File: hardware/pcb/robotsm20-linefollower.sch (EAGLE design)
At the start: 141 parts, among them Q5 BSS138LT3G, Q6 BSS138LT3G, Q7 BSS138LT3G, Q8 BSS138LT3G, U1 STM32F405RG

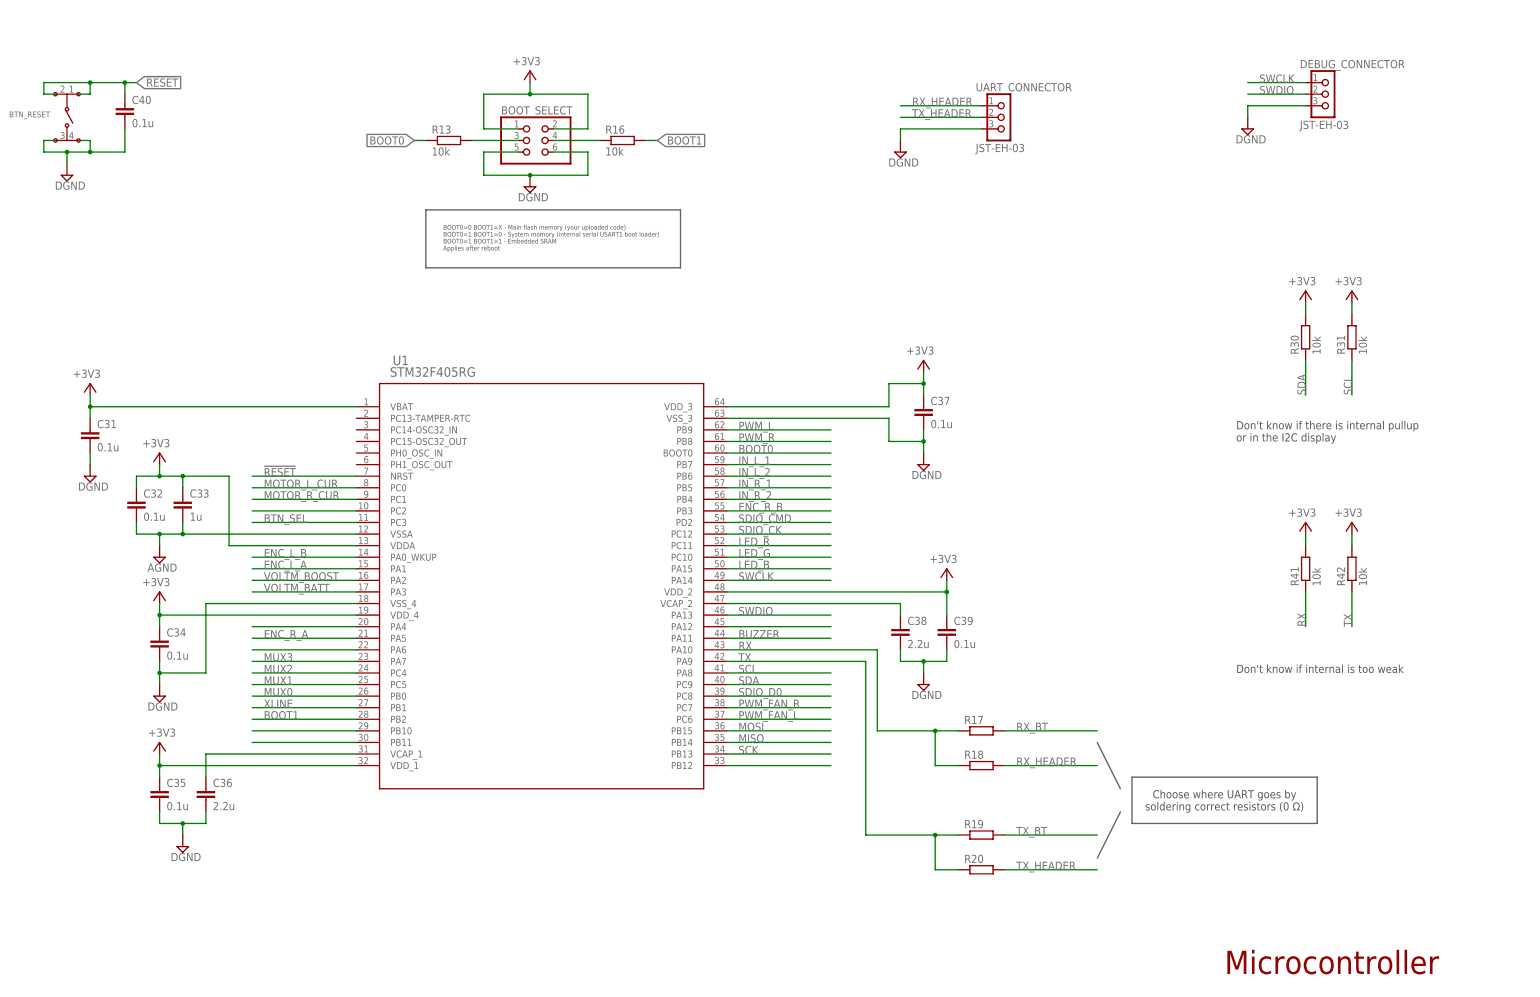
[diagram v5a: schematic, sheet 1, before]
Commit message: Change resistor and pinheader to dipswitch for RXTXBT and BOOT12
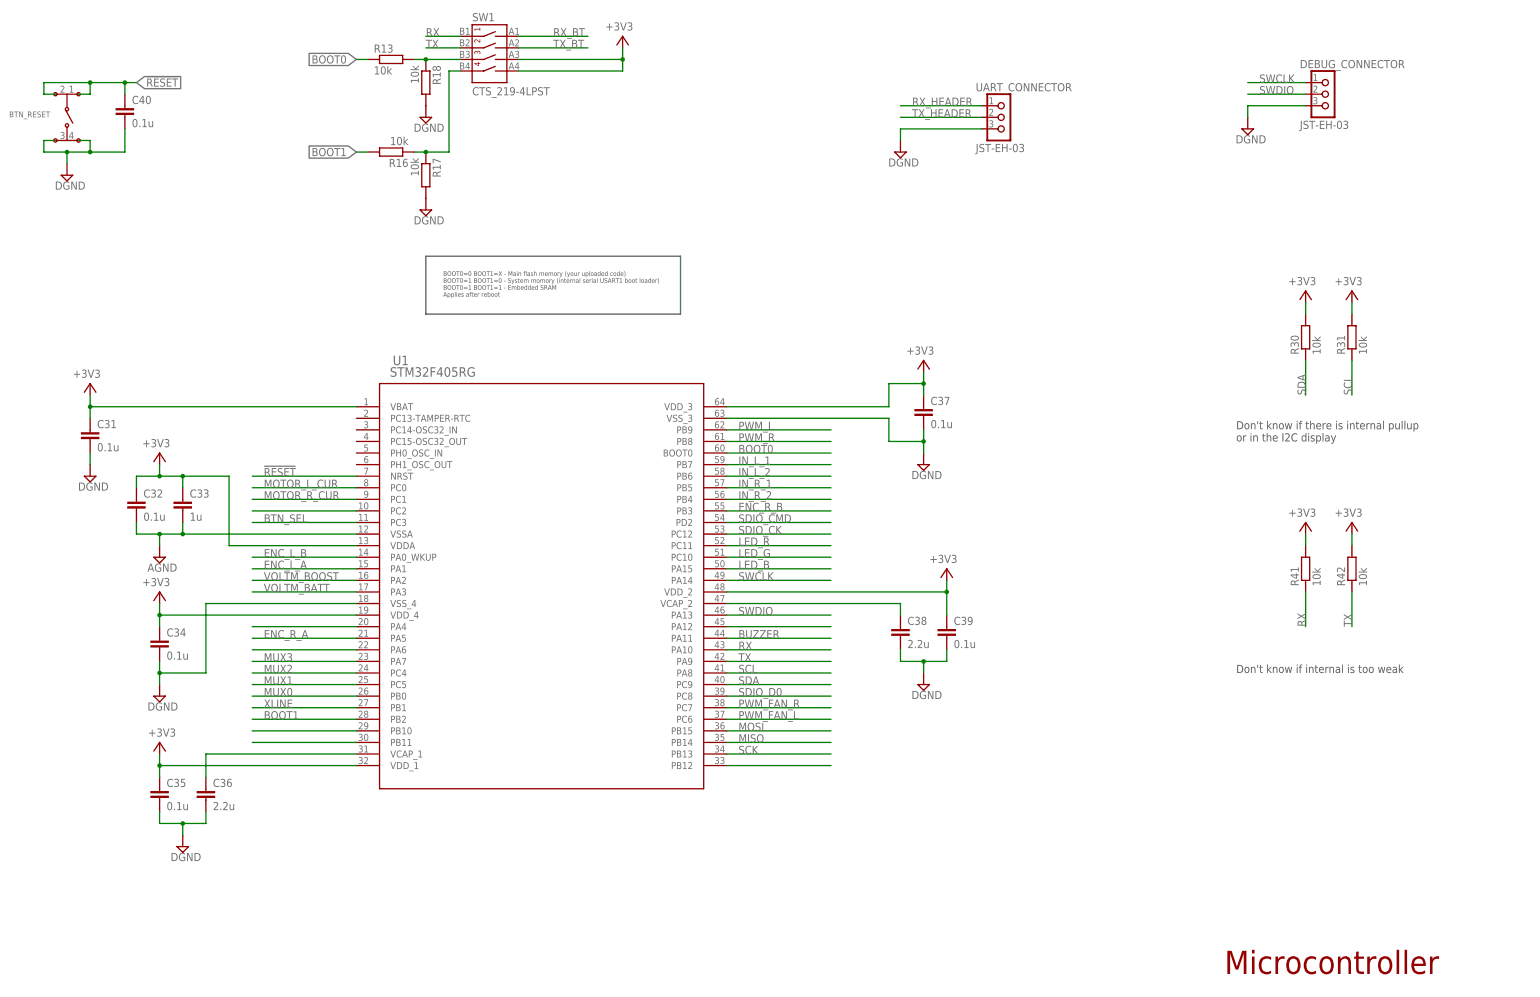
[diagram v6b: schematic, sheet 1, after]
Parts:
- removed BOOT_SELECT: (no value), CASE-Pinhead:PINHD-2X3
- removed R19, R20: (no value), rcl:R-EU_R0603
- added SW1: CTS_219-4LPST, CASE-Switches:CTS_219-4LPST
- R17, R18: value (none) -> 10k
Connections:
- net +3V3: now also SW1.A3, SW1.A4; no longer BOOT_SELECT.1, BOOT_SELECT.2
- net DGND: now also R17.1, R18.1; no longer BOOT_SELECT.5, BOOT_SELECT.6
- net N$26: now also R17.2, SW1.B4; no longer BOOT_SELECT.4
- net N$34: now also R18.2, SW1.B3; no longer BOOT_SELECT.3
- net RX: now also SW1.B1; no longer R17.2, R18.2
- net RX_BT: now also SW1.A1; no longer R17.1
- net RX_HEADER: no longer R18.1
- net TX: now also SW1.B2; no longer R19.2, R20.2
- net TX_BT: now also SW1.A2; no longer R19.1
- net TX_HEADER: no longer R20.1
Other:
- note removed: "Choose where UART goes by soldering correct resistors (0 Ω)"
- moved on the sheet: R13, R16, R17, R18

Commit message: Routed new dipswitch
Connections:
- removed net RX_HEADER: UART_CONNECTOR.1
- removed net TX_HEADER: UART_CONNECTOR.2
- net RX: now also UART_CONNECTOR.1
- net TX: now also UART_CONNECTOR.2
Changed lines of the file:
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@@
 <attribute name="VALUE" x="-167.767" y="70.485" size="1.778" layer="96"/>
 </instance>
-<instance part="SUPPLY48" gate="G$1" x="17.78" y="78.74" smashed="yes" grouprefs="UART">
-<attribute name="VALUE" x="15.113" y="75.565" size="1.778" layer="96"/>
+<instance part="SUPPLY48" gate="G$1" x="25.4" y="78.74" smashed="yes" grouprefs="UART">
+<attribute name="VALUE" x="22.733" y="75.565" size="1.778" layer="96"/>
 </instance>
 <instance part="SUPPLY49" gate="G$1" x="93.98" y="83.82" smashed="yes" grouprefs="DEBUG">
@@
 <attribute name="VALUE" x="-89.027" y="62.865" size="1.778" layer="96"/>
 </instance>
-<instance part="SW1" gate="G$1" x="-76.2" y="106.68" smashed="yes" rot="R270">
+<instance part="SW1" gate="G$1" x="-76.2" y="106.68" smashed="yes" rot="R270" grouprefs="MODE">
 <attribute name="NAME" x="-76.2" y="107.442" size="1.778" layer="95" font="vector"/>
 <attribute name="VALUE" x="-76.2" y="92.964" size="1.778" layer="96" font="vector" align="top-left"/>
@@
 <pinref part="SW1" gate="G$1" pin="B1"/>
 </segment>
+<segment>
+<pinref part="UART_CONNECTOR" gate="G$1" pin="1"/>
+<wire x1="35.56" y1="88.9" x2="25.4" y2="88.9" width="0.1524" layer="91" grouprefs="UART"/>
+<label x="27.94" y="88.9" size="1.778" layer="95" grouprefs="UART"/>
+</segment>
 </net>
 <net name="BUZZER" class="0">
@@
 <pinref part="SW1" gate="G$1" pin="B2"/>
 </segment>
+<segment>
+<pinref part="UART_CONNECTOR" gate="G$1" pin="2"/>
+<wire x1="35.56" y1="86.36" x2="25.4" y2="86.36" width="0.1524" layer="91" grouprefs="UART"/>
+<label x="27.94" y="86.36" size="1.778" layer="95" grouprefs="UART"/>
+</segment>
 </net>
 <net name="SDIO_D0" class="0">
@@
 <label x="-58.42" y="104.14" size="1.778" layer="95" grouprefs="MODE"/>
 <pinref part="SW1" gate="G$1" pin="A1"/>
-</segment>
-</net>
-<net name="RX_HEADER" class="0">
-<segment>
-<pinref part="UART_CONNECTOR" gate="G$1" pin="1"/>
-<wire x1="35.56" y1="88.9" x2="17.78" y2="88.9" width="0.1524" layer="91" grouprefs="UART"/>
-<label x="20.32" y="88.9" size="1.778" layer="95" grouprefs="UART"/>
-</segment>
-</net>
-<net name="TX_HEADER" class="0">
-<segment>
-<pinref part="UART_CONNECTOR" gate="G$1" pin="2"/>
-<wire x1="35.56" y1="86.36" x2="17.78" y2="86.36" width="0.1524" layer="91" grouprefs="UART"/>
-<label x="20.32" y="86.36" size="1.778" layer="95" grouprefs="UART"/>
 </segment>
 </net>
@@
 <junction x="-86.36" y="78.74" grouprefs="MODE"/>
 <pinref part="SW1" gate="G$1" pin="B4"/>
-<wire x1="-78.74" y1="96.52" x2="-81.28" y2="96.52" width="0.1524" layer="91"/>
-<wire x1="-81.28" y1="96.52" x2="-81.28" y2="78.74" width="0.1524" layer="91"/>
+<wire x1="-78.74" y1="96.52" x2="-81.28" y2="96.52" width="0.1524" layer="91" grouprefs="MODE"/>
+<wire x1="-81.28" y1="96.52" x2="-81.28" y2="78.74" width="0.1524" layer="91" grouprefs="MODE"/>
 </segment>
 </net>
@@
 <wire x1="-86.36" y1="99.06" x2="-88.9" y2="99.06" width="0.1524" layer="91" grouprefs="MODE"/>
 <pinref part="SW1" gate="G$1" pin="B3"/>
-<wire x1="-78.74" y1="99.06" x2="-86.36" y2="99.06" width="0.1524" layer="91"/>
-<junction x="-86.36" y="99.06"/>
+<wire x1="-78.74" y1="99.06" x2="-86.36" y2="99.06" width="0.1524" layer="91" grouprefs="MODE"/>
+<junction x="-86.36" y="99.06" grouprefs="MODE"/>
 </segment>
 </net>
@@
 <segment>
 <pinref part="+3V15" gate="G$1" pin="+3V3"/>
-<wire x1="-43.18" y1="101.6" x2="-43.18" y2="99.06" width="0.1524" layer="91"/>
+<wire x1="-43.18" y1="101.6" x2="-43.18" y2="99.06" width="0.1524" layer="91" grouprefs="MODE"/>
 <pinref part="SW1" gate="G$1" pin="A3"/>
-<wire x1="-43.18" y1="99.06" x2="-66.04" y2="99.06" width="0.1524" layer="91"/>
+<wire x1="-43.18" y1="99.06" x2="-66.04" y2="99.06" width="0.1524" layer="91" grouprefs="MODE"/>
 <pinref part="SW1" gate="G$1" pin="A4"/>
-<wire x1="-66.04" y1="96.52" x2="-43.18" y2="96.52" width="0.1524" layer="91"/>
-<wire x1="-43.18" y1="96.52" x2="-43.18" y2="99.06" width="0.1524" layer="91"/>
-<junction x="-43.18" y="99.06"/>
+<wire x1="-66.04" y1="96.52" x2="-43.18" y2="96.52" width="0.1524" layer="91" grouprefs="MODE"/>
+<wire x1="-43.18" y1="96.52" x2="-43.18" y2="99.06" width="0.1524" layer="91" grouprefs="MODE"/>
+<junction x="-43.18" y="99.06" grouprefs="MODE"/>
 </segment>
 </net>
@@
 <segment>
 <pinref part="SUPPLY48" gate="G$1" pin="DGND"/>
-<wire x1="17.78" y1="81.28" x2="17.78" y2="83.82" width="0.1524" layer="91"/>
+<wire x1="25.4" y1="81.28" x2="25.4" y2="83.82" width="0.1524" layer="91" grouprefs="UART"/>
 <pinref part="UART_CONNECTOR" gate="G$1" pin="3"/>
-<wire x1="17.78" y1="83.82" x2="35.56" y2="83.82" width="0.1524" layer="91"/>
-</segment>
-<segment>
+<wire x1="25.4" y1="83.82" x2="35.56" y2="83.82" width="0.1524" layer="91" grouprefs="UART"/>
+</segment>
+<segment>

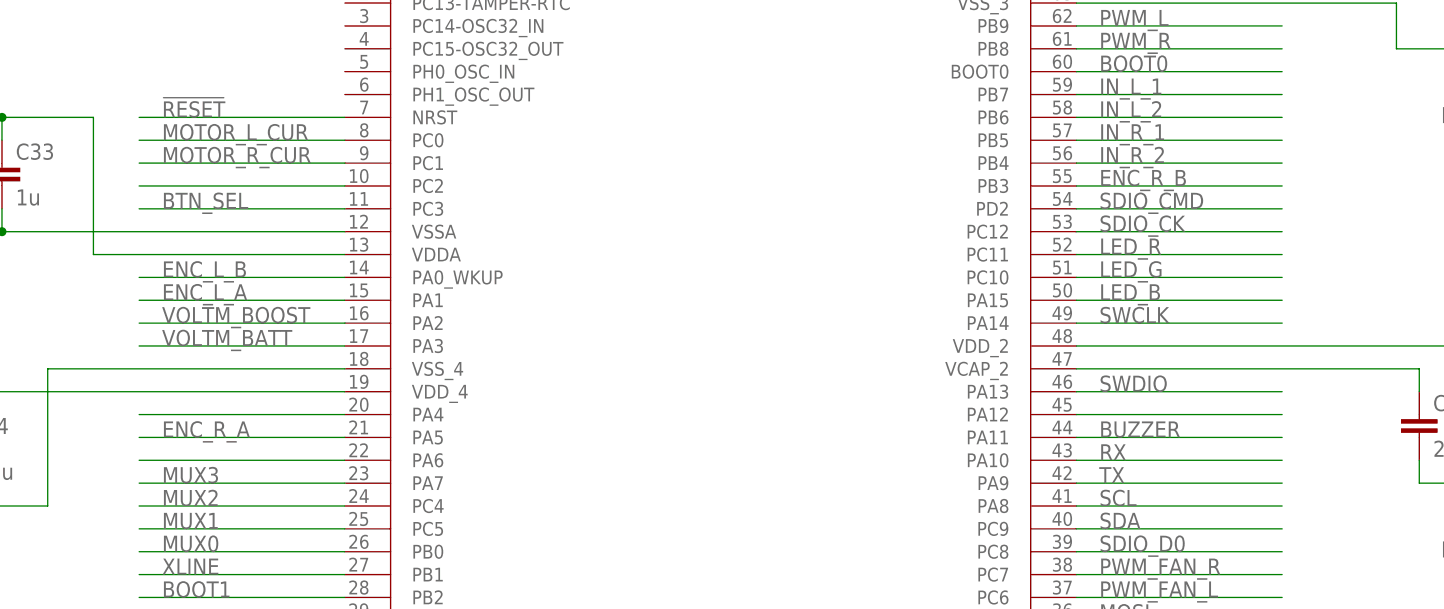
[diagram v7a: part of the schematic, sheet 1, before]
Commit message: Switched RL encoder pins
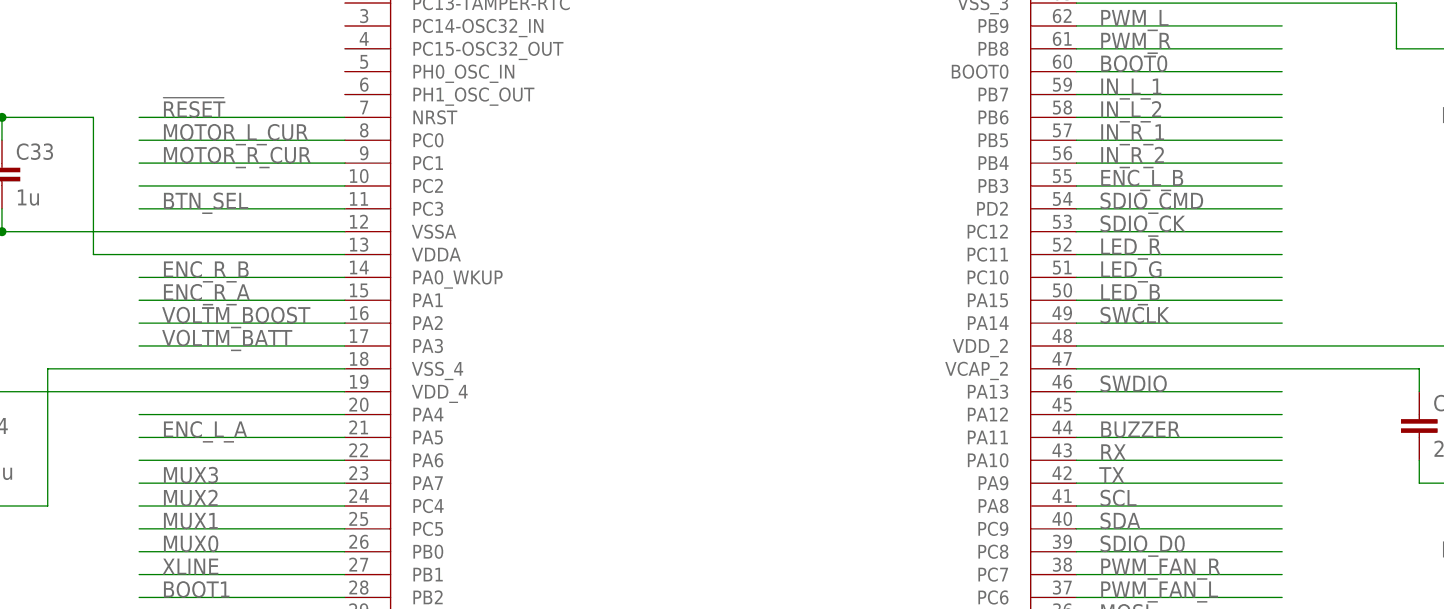
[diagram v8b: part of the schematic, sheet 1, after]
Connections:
- net ENC_L_A: now also U1.PA5; no longer U1.PA1
- net ENC_L_B: now also U1.PB3; no longer U1.PA0_WKUP
- net ENC_R_A: now also U1.PA1; no longer U1.PA5
- net ENC_R_B: now also U1.PA0_WKUP; no longer U1.PB3
